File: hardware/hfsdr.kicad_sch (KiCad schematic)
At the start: 56 parts, among them J1 USB_C_Receptacle_USB2.0_16P, SW1 RST, SW2 BOOT0, SW4 EC12E2430803, U3 CH32V30xRxTx

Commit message: hardware fix: MCO MCK + MS5351 VDD
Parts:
- added JP1: MCK_OLD, symbol Jumper:SolderJumper_2_Open
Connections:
- net PA8 is gone; now on net MCK: TP18.1, U3.41 (PA8)
- net MCK: now also JP1.2 (B); no longer U3.37 (PC6)
- new net MCK_OLD: JP1.1 (A), U3.37 (PC6)
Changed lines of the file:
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@@
 	)
 	(junction
+		(at 120.65 85.09)
+		(diameter 0)
+		(color 0 0 0 0)
+	)
+	(junction
 		(at 158.75 46.99)
 		(diameter 0)
@@
 	)
 	(junction
+		(at 127 87.63)
+		(diameter 0)
+		(color 0 0 0 0)
+	)
+	(junction
 		(at 261.62 270.51)
 		(diameter 0)
@@
 	(wire
 		(pts
-			(xy 119.38 87.63) (xy 138.43 87.63)
+			(xy 119.38 87.63) (xy 127 87.63)
 		)
 		(stroke
@@
 	(wire
 		(pts
+			(xy 120.65 81.28) (xy 120.65 85.09)
+		)
+		(stroke
+			(width 0)
+			(type default)
+		)
+	)
+	(wire
+		(pts
 			(xy 158.75 46.99) (xy 158.75 49.53)
 		)
@@
 	(wire
 		(pts
+			(xy 101.6 81.28) (xy 120.65 81.28)
+		)
+		(stroke
+			(width 0)
+			(type default)
+		)
+	)
+	(wire
+		(pts
 			(xy 153.67 49.53) (xy 156.21 49.53)
 		)
@@
 	(wire
 		(pts
+			(xy 119.38 85.09) (xy 120.65 85.09)
+		)
+		(stroke
+			(width 0)
+			(type default)
+		)
+	)
+	(wire
+		(pts
 			(xy 332.74 68.58) (xy 332.74 64.77)
 		)
@@
 	(wire
 		(pts
+			(xy 127 87.63) (xy 138.43 87.63)
+		)
+		(stroke
+			(width 0)
+			(type default)
+		)
+	)
+	(wire
+		(pts
 			(xy 373.38 200.66) (xy 355.6 200.66)
 		)
@@
 	(wire
 		(pts
+			(xy 120.65 85.09) (xy 127 85.09)
+		)
+		(stroke
+			(width 0)
+			(type default)
+		)
+	)
+	(wire
+		(pts
 			(xy 168.91 85.09) (xy 180.34 85.09)
 		)
@@
 	(wire
 		(pts
+			(xy 127 85.09) (xy 127 87.63)
+		)
+		(stroke
+			(width 0)
+			(type default)
+		)
+	)
+	(wire
+		(pts
 			(xy 361.95 151.13) (xy 361.95 139.7)
 		)
@@
 		)
 	)
-	(global_label "MCK"
-		(shape input)
-		(at 171.45 82.55 0)
-		(fields_autoplaced yes)
-		(effects
-			(font
-				(size 1.27 1.27)
-			)
-			(justify left)
-		)
-		(property "Intersheetrefs" "${INTERSHEET_REFS}"
-			(at 178.4266 82.55 0)
-			(effects
-				(font
-					(size 1.27 1.27)
-				)
-				(justify left)
-				(hide yes)
-			)
-		)
-	)
 	(global_label "CS"
 		(shape input)
@@
 		)
 	)
+	(global_label "MCK_OLD"
+		(shape input)
+		(at 93.98 81.28 180)
+		(fields_autoplaced yes)
+		(effects
+			(font
+				(size 1.27 1.27)
+			)
+			(justify right)
+		)
+		(property "Intersheetrefs" "${INTERSHEET_REFS}"
+			(at 82.4072 81.28 0)
+			(effects
+				(font
+					(size 1.27 1.27)
+				)
+				(justify right)
+				(hide yes)
+			)
+		)
+	)
 	(global_label "ENC_A"
 		(shape input)
@@
 		)
 	)
+	(global_label "MCK_OLD"
+		(shape input)
+		(at 171.45 82.55 0)
+		(fields_autoplaced yes)
+		(effects
+			(font
+				(size 1.27 1.27)
+			)
+			(justify left)
+		)
+		(property "Intersheetrefs" "${INTERSHEET_REFS}"
+			(at 183.0228 82.55 0)
+			(effects
+				(font
+					(size 1.27 1.27)
+				)
+				(justify left)
+				(hide yes)
+			)
+		)
+	)
 	(global_label "PB2"
 		(shape input)
@@
 		)
 	)
+	(global_label "MCK"
+		(shape input)
+		(at 119.38 85.09 180)
+		(fields_autoplaced yes)
+		(effects
+			(font
+				(size 1.27 1.27)
+			)
+			(justify right)
+		)
+		(property "Intersheetrefs" "${INTERSHEET_REFS}"
+			(at 112.4034 85.09 0)
+			(effects
+				(font
+					(size 1.27 1.27)
+				)
+				(justify right)
+				(hide yes)
+			)
+		)
+	)
 	(global_label "ENC_B"
 		(shape input)
@@
 					(unit 1)
 				)
+			)
+		)
+	)
+	(symbol
+		(lib_id "Jumper:SolderJumper_2_Open")
+		(at 97.79 81.28 0)
+		(unit 1)
+		(exclude_from_sim no)
+		(in_bom no)
+		(on_board yes)
+		(dnp no)
+		(fields_autoplaced yes)
+		(property "Reference" "JP1"
+			(at 97.79 74.93 0)
+			(effects
+				(font
+					(size 1.27 1.27)
+				)
+			)
+		)
+		(property "Value" "MCK_OLD"
+			(at 97.79 77.47 0)
+			(effects
+				(font
+					(size 1.27 1.27)
+				)
+			)
+		)
+		(property "Footprint" ""
+			(at 97.79 81.28 0)
+			(effects
+				(font
+					(size 1.27 1.27)
+				)
+				(hide yes)
+			)
+		)
+		(property "Datasheet" "~"
+			(at 97.79 81.28 0)
+			(effects
+				(font
+					(size 1.27 1.27)
+				)
+				(hide yes)
+			)
+		)
+		(property "Description" "Solder Jumper, 2-pole, open"
+			(at 97.79 81.28 0)
+			(effects
+				(font
+					(size 1.27 1.27)
+				)
+				(hide yes)
+			)
+		)
+		(pin "2"
+		)
+		(pin "1"
+		)
+		(instances
+			(project ""
+				(path "/a11445ed-c3bd-4d1c-a039-1c09b0dceab8"
+					(reference "JP1")
+					(unit 1)
+				)

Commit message: feat: pcb edits
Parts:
- JP1: footprint (none) -> Jumper:SolderJumper-2_P1.3mm_Open_RoundedPad1.0x1.5mm
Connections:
- net +3.3V: now also FPC1.15, FPC1.16, FPC1.2; no longer FPC1.17, FPC1.3, FPC1.4
- net CS: now also FPC1.11; no longer FPC1.8
- net GND: now also FPC1.13, FPC1.14, FPC1.17, FPC1.7; no longer FPC1.12, FPC1.5, FPC1.6
- net PC10: now also FPC1.4; no longer FPC1.15
- net PC11: now also FPC1.8; no longer FPC1.11
- net RS: now also FPC1.12; no longer FPC1.7
- net SCL: now also FPC1.6; no longer FPC1.13
- net SCL_SCK: now also FPC1.10; no longer FPC1.9
- net SDA: now also FPC1.5; no longer FPC1.14
- net SDA_MOSI: now also FPC1.9; no longer FPC1.10
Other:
- moved on the sheet: FPC1
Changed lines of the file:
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@@
 	)
 	(junction
+		(at 355.6 190.5)
+		(diameter 0)
+		(color 0 0 0 0)
+	)
+	(junction
 		(at 332.74 38.1)
 		(diameter 0)
@@
 	)
 	(junction
-		(at 355.6 190.5)
+		(at 341.63 132.08)
 		(diameter 0)
 		(color 0 0 0 0)
 	)
 	(junction
-		(at 341.63 132.08)
+		(at 360.68 69.85)
 		(diameter 0)
 		(color 0 0 0 0)
 	)
 	(junction
-		(at 360.68 69.85)
+		(at 127 87.63)
 		(diameter 0)
 		(color 0 0 0 0)
 	)
 	(junction
-		(at 127 87.63)
+		(at 355.6 185.42)
 		(diameter 0)
 		(color 0 0 0 0)
@@
 	)
 	(junction
-		(at 360.68 62.23)
+		(at 355.6 195.58)
 		(diameter 0)
 		(color 0 0 0 0)
 	)
 	(junction
-		(at 236.22 262.89)
+		(at 360.68 62.23)
 		(diameter 0)
 		(color 0 0 0 0)
 	)
 	(junction
-		(at 355.6 195.58)
+		(at 236.22 262.89)
 		(diameter 0)
 		(color 0 0 0 0)
@@
 	(wire
 		(pts
+			(xy 355.6 185.42) (xy 355.6 187.96)
+		)
+		(stroke
+			(width 0)
+			(type default)
+		)
+	)
+	(wire
+		(pts
 			(xy 172.72 110.49) (xy 168.91 110.49)
 		)
@@
 			"////eQAAAA4AIAD/////////fwAAAAAAAACAeQAAAA8AIAD/////////fwAAAIAQAAAAeQAAABAA"
 			"IAD//39///9//wAAAAAAAAAAeQAAABEAIAD////////vf////////+//eQAAABIAIAAAPAAAADgA"
-			"AABAAAAAQgAAeQAAABMAIAB3JAAAKVMAAEg+AABIQgAAeQAAABQAIAAEAAAA//8AAA=="
+			"AABAAAAAQgAAeQAAABMAIAB3JAAAKVMAAEg+AABIQgAAeQAAABQAIAAEAAAA//8AAAAAAAAAAAAA"
+			"AAAAAAAAAAAAAAAAAAAAAAAAAAAAAAAAAAAAAAAAAAAAAAAAAAAAAAAAAAAAAAAAAAAAAAAAAAAA"
+			"AAAAAAAAAAAAAAAAAAAAAAAAAAAAAAAAAAAAAAAAAAAAAAAAAAAAAAAAAAAAAAAAAAAAAAAAAAAA"
+			"AAAAAAAAAAAAAAAAAAAAAAAAAAAAAAAAAAAAAAAAAAAAAAAAAAAAAAAAAAAAAAAAAAAAAAAAAAAA"
+			"AAAAAAAAAAAAAAAAAAAAAAAAAAAAAAAAAAAAAAAAAAAAAAAAAAAAAAAAAAAAAAAAAAAAAAAAAAAA"
+			"AAAAAAAAAAAAAAAAAAAAAAAAAAAAAAAAAAAAAAAAAAAAAAAAAAAAAAAAAAAAAAAAAAAAAAAAAAAA"
+			"AAAAAAAAAAAAAAAAAAAAAAAAAAAAAAAAAAAAAAAAAAAAAAAAAAAAAAAAAAAAAAAAAAAAAAAAAAAA"
+			"AAAAAAAAAAAAAAAAAAAAAAAAAAAAAAAAAAAAAAAAAAAAAAAAAAAAAAAAAAAAAAAAAAAAAAAAAAAA"
+			"AAAAAAAAAAAAAAAAAAAAAAAAAAAAAAAAAAAAAAAAAAAAAAAAAAAAAAAAAAAAAAAAAAAAAAAAAAAA"
+			"AAAAAAAAAAAAAAAAAAAAAAAAAAAAAAAAAAAAAAAAAAAAAAAAAAAAAAAAAAAAAAAAAAAAAAAAAAAA"
+			"AAAAAAAAAAAAAAAAAAAAAAAAAAAAAAAAAAAAAAAAAAAAAAAAAAAAAAAAAAAAAAAAAAAAAAAAAAAA"
+			"AAAAAAAAAAAAAAAAAAAAAAAAAAAAAAAAAAAAAAAAAAAAAAAAAAAAAAAAAAAAAAAAAAAAAAAAAAAA"
+			"AAAAAAAAAAAAAAAAAAAAAAAAAAAAAAAAAAAAAAAAAAAAAAAAAAAAAAAAAAAAAAAAAAAAAAAAAAAA"
+			"AAAAAAAAAAAAAAAAAAAAAAAAAAAAAAAAAAAAAAAAAAAAAAAAAAAAAAAAAAAAAAAAAAAAAAAAAAAA"
+			"AAAAAAAAAAAAAAAAAAAAAAAAAAAAAAAAAAAAAAAAAAAAAAAAAAAAAAAAAAAAAAAAAAAAAAAAAAAA"
+			"AAAAAAAAAAAAAAAAAAAAAAAAAAAAAAAAAAAAAAAAAAAAAAAAAAAAAAAAAAAAAAAAAAAAAAAAAAAA"
+			"AAAAAAAAAAAAAAAAAAAAAAAAAAAAAAAAAAAAAAAAAAAAAAAAAAAAAAAAAAAAAAAAAAAAAAAAAAAA"
+			"AAAAAAAAAAAAAAAAAAAAAAAAAAAAAAAAAAAAAAAAAAAAAAAAAAAAAAAAAAAAAAAAAAAAAAAAAAAA"
+			"AAAAAAAAAAAAAAAAAAAAAAAAAAAAAAAAAAAAAAAAAAAAAAAAAAAAAAAAAAAAAAAAAA=="
 		)
 	)
@@
 			"AAAAAAAAAAAAAAAAAAAAAAAAAAAAAAAAAAAAAAAAAAAAAAAAAAAAAAAAAAAAAAAAAAAAAAAAAAAA"
 			"AAAAAAAAAAAAAAAAAAAAAAAAAAAAAAAAAAAAAAAAAAAAAAAAAAAAAAAAAAAAAAAAAAAAAAAAAAAA"
+			"AAAAAAAAAAAAAAAAAAAAAAAAAAAAAAAAAAAAAAAAAAAAAAAAAAAAAAAAAAAAAAAAAAAAAAAAAAAA"
+			"AAAAAAAAAAAAAAAAAAAAAAAAAAAAAAAAAAAAAAAAAAAAAAAAAAAAAAAAAAAAAAAAAAAAAAAAAAAA"
+			"AAAAAAAAAAAAAAAAAAAAAAAAAAAAAAAAAAAAAAAAAAAAAAAAAAAAAAAAAAAAAAAAAAAAAAAAAAAA"
+			"AAAAAAAAAAAAAAAAAAAAAAAAAAAAAAAAAAAAAAAAAAAAAAAAAAAAAAAAAAAAAAAAAAAAAAAAAAAA"
+			"AAAAAAAAAAAAAAAAAAAAAAAAAAAAAAAAAAAAAAAAAAAAAAAAAAAAAAAAAAAAAAAAAAAAAAAAAAAA"
+			"AAAAAAAAAAAAAAAAAAAAAAAAAAAAAAAAAAAAAAAAAAAAAAAAAAAAAAAAAAAAAAAAAAAAAAAAAAAA"
+			"AAAAAAAAAAAAAAAAAAAAAAAAAAAAAAAAAAAAAAAAAAAAAAAAAAAAAAAAAAAAAAAAAAAAAAAAAAAA"
+			"AAAAAAAAAAAAAAAAAAAAAAAAAAAAAAAAAAAAAAAAAAAAAAAAAAAAAAAAAAAAAAAAAAAAAAAAAAAA"
+			"AAAAAAAAAAAAAAAAAAAAAAAAAAAAAAAAAAAAAAAAAAAAAAAAAAAAAAAAAAAAAAAAAAAAAAAAAAAA"
+			"AAAAAAAAAAAAAAAAAAAAAAAAAAAAAAAAAAAAAAAAAAAAAAAAAAAAAAAAAAAAAAAAAAAAAAAAAAAA"
+			"AAAAAAAAAAAAAAAAAAAAAAAAAAAAAAAAAAAAAAAAAAAAAAAAAAAAAAAAAAAAAAAAAAAAAAAAAAAA"
+			"AAAAAAAAAAAAAAAAAAAAAAAAAAAAAAAAAAAAAAAAAAAAAAAAAAAAAAAAAAAAAAAAAAAAAAAAAAAA"
+			"AAAAAAAAAAAAAAAAAAAAAAAAAAAAAAAAAAAAAAAAAAAAAAAAAAAAAAAAAAAAAAAAAAAAAAAAAAAA"
+			"AAAAAAAAAAAAAAAAAAAAAAAAAAAAAAAAAAAAAAAAAAAAAAAAAAAAAAAAAAAAAAAAAAAAAAAAAAAA"
+			"AAAAAAAAAAAAAAAAAAAAAAAAAAAAAAAAAAAAAAAAAAAAAAAAAAAAAAAAAAAAAAAAAAAAAAAAAAAA"
+			"AAAAAAAAAAAAAAAAAAAAAAAAAAAAAAAAAAAAAAAAAAAAAAAAAAAAAAAAAAAAAAAAAAAAAAAAAAAA"
+			"AAAAAAAAAAAAAAAAAAAAAAAAAAAAAAAAAAAAAAAAAAAAAAAAAAAAAAAAAAAAAAAAAAAAAAAAAAAA"
+			"AAAAAAAAAAAAAAAAAAAAAAAAAAAAAAAAAAAAAAAAAAAAAAAAAAAAAAAAAAAAAAAAAAAAAAAAAAAA"
 			"AAAAAAAAAAAAAAAAAAAAAAAAAAAAAAAAAAAAAAAAAAAAAAAAAA=="
 		)
@@
 			"gEQAEREAAEcAAAAngEQAEAAAACaARAAiIgAARwAAAAmARAAVAAAAJ4BEABAyAAAIAAAABwEAAEcA"
 			"AAAogEQAAQAAAD4CRAAAAAAARwAAAAiARAABAAAAKIBEAAAAAABHAAAAKYBEAAEAAAAHgEQAAAAA"
-			"AFsAAAAqgEQAAQAAAD4BYAAAAAAAKYBEAAAAAABHAA=="
+			"AFsAAAAqgEQAAQAAAD4BYAAAAAAAKYBEAAAAAABHAAAAAAAAAAAAAAAAAAAAAAAAAAAAAAAAAAAA"
+			"AAAAAAAAAAAAAAAAAAAAAAAAAAAAAAAAAAAAAAAAAAAAAAAAAAAAAAAAAAAAAAAAAAAAAAAAAAAA"
+			"AAAAAAAAAAAAAAAAAAAAAAAAAAAAAAAAAAAAAAAAAAAAAAAAAAAAAAAAAAAAAAAAAAAAAAAAAAAA"
+			"AAAAAAAAAAAAAAAAAAAAAAAAAAAAAAAAAAAAAAAAAAAAAAAAAAAAAAAAAAAAAAAAAAAAAAAAAAAA"
+			"AAAAAAAAAAAAAAAAAAAAAAAAAAAAAAAAAAAAAAAAAAAAAAAAAAAAAAAAAAAAAAAAAAAAAAAAAAAA"
+			"AAAAAAAAAAAAAAAAAAAAAAAAAAAAAAAAAAAAAAAAAAAAAAAAAAAAAAAAAAAAAAAAAAAAAAAAAAAA"
+			"AAAAAAAAAAAAAAAAAAAAAAAAAAAAAAAAAAAAAAAAAAAAAAAAAAAAAAAAAAAAAAAAAAAAAAAAAAAA"
+			"AAAAAAAAAAAAAAAAAAAAAAAAAAAAAAAAAAAAAAAAAAAAAAAAAAAAAAAAAAAAAAAAAAAAAAAAAAAA"
+			"AAAAAAAAAAAAAAAAAAAAAAAAAAAAAAAAAAAAAAAAAAAAAAAAAAAAAAAAAAAAAAAAAAAAAAAAAAAA"
+			"AAAAAAAAAAAAAAAAAAAAAAAAAAAAAAAAAAAAAAAAAAAAAAAAAAAAAAAAAAAAAAAAAAAAAAAAAAAA"
+			"AAAAAAAAAAAAAAAAAAAAAAAAAAAAAAAAAAAAAAAAAAAAAAAAAAAAAAAAAAAAAAAAAAAAAAAAAAAA"
+			"AAAAAAAAAAAAAAAAAAAAAAAAAAAAAAAAAAAAAAAAAAAAAAAAAAAAAAAAAAAAAAAAAAAAAAAAAAAA"
+			"AAAAAAAAAAAAAAAAAAAAAAAAAAAAAAAAAAAAAAAAAAAAAAAAAAAAAAAAAAAAAAAAAAAAAAAAAAAA"
+			"AAAAAAAAAAAAAAAAAAAAAAAAAAAAAAAAAAAAAAAAAAAAAAAAAAAAAAAAAAAAAAAAAAAAAAAAAAAA"
+			"AAAAAAAAAAAAAAAAAAAAAAAAAAAAAAAAAAAAAAAAAAAAAAAAAAAAAAAAAAAAAAAAAAAAAAAAAAAA"
+			"AAAAAAAAAAAAAAAAAAAAAAAAAAAAAAAAAAAAAAAAAAAAAAAAAAAAAAAAAAAAAAAAAAAAAAAAAAAA"
+			"AAAAAAAAAAAAAAAAAAAAAAAAAAAAAAAAAAAAAAAAAAAAAAAAAAAAAAAAAAAAAAAAAAAAAAAAAAAA"
+			"AAAAAAAAAAAAAAAAAAAAAAAAAAAAAAAAAAAAAAAAAAAAAAAAAAAAAAAAAAAAAAAAAAAAAAAAAAAA"
+			"AAAAAAAAAAAAAAAAAAAAAAAAAAAAAAAAAAAAAAAAAA=="
 		)
 	)
@@
 			"/yf/fwAA8N//J/9/AACQ4P8n/38AADDh/yf/fwAAEPj/J/9/AADA+P8n/38AAGD5/yf/fwAAEPr/"
 			"J/9/AACw+v8n/38AAGD7/yf/fwAAAPz/J/9/AACw/P8n/38AAFD9/yf/fwAAIP7/J/9/AADA/v8n"
-			"/38AAJD//yf/fwAAMAAAKP9/AADwAAAo/38AAJABACj/fw=="
+			"/38AAJD//yf/fwAAMAAAKP9/AADwAAAo/38AAJABACj/f0l2QXIvVDV1ZHErdFVldHhKbGdadDRI"
+			"WHI4TU16LzZKNjF2MHllTUdmVnNjdFhUeXh4cy9yR2c4R1JaSzh0ZEczYTlSOCt5c3VqbzRQaEYz"
+			"dW9CY0dyMTBUa2duR2Y4VjVXRlkzQXpRZU45N0RBWmZlMy9IVXNnd1VBWURrTzZBY0hOd1JxUklD"
+			"VGpmdTZPWlcrMTNUTTFtVkhVbWxoeDhrelhMV0dyWW5ienByZW12bzR5ZjZwOW4wU2dpNGp2V3lx"
+			"RGhRWGRoN2xaZjh1Q2ZzNk1LaWcxMUNYeWo5aDBzSEJHZ2RnaTdLeWlqNWtFRzQxZk5YUEhjU2dm"
+			"bjU0M2VFWDVWSmpCSTVDMkJIRmNOSlg2b0NqaXQ5L2t3NGJWOWgvZEtISG1NTEJVNlh6MWltT1hx"
+			"T3pxOXJCRDRGQUlLcEVxOCtpN3U4LytNWnI5L0x1dWlDN2RzRDdTUlVpVzd1cm9tTUR6eWVvQ1Z1"
+			"bk1oMXRBdWNtOW9RNi9rSlEzTmVpMlN2Q04vdXV4NUJSNDhhTjl1cmZ5ZG44Qzg0dHJEMis4UllI"
+			"b2l6U01ML2dOd3hHTm0zZnZ2ek0wV0xFcmgxYUNMelRDeTZmQ240N2ZtcGRRZnRCL2F5ODl5VjZq"
+			"MmovNHFmTjI1ZDRPaFdQRFpBdEZ2enBYUHg2VTNlUCtqMm1PTEpWMXg3MUsybUo0RmJqLzV6OVVT"
+			"L1NwOXIzZVpzKzdLdHpRZEplRzZxYU5zdG1aa280QU56WTJ2b2oybUdFbmVlUXRvdHZYSkhkREx5"
+			"WU9YTkdQZFFjUm1qQ0pZWXBOM21yN2xGRUwzZCsxeEg4K1kxeFl3RUdBRlFCRXg5TFg3MnNHTDJK"
+			"cys4clhEU2ViMTF1L2xRK3RXcUI4c0pMVmxtMk1ZaGh1bWI0NEo5MGYyeGRybCtNaTlvdFhSeklG"
+			"SlEyQURBY3E5ZFhmTnlMMjdLSmlubk5wRWcwVjZYRkFNY3hrZ1NSTG1aa2pOZTNKcG80azEwNmtF"
+			"NG1GYnJiV0Nab2l5SWduazE2eWNvMW02VVlEZ1NKQ1FXWW5oRm1ZVUU0TkNMYXR1TzFiNGovUi9h"
+			"U1F5QytDclQ1cklLUTNYN2lNVUZEeDhVRnJnay8vdVRJbml1Lzd1cjFTZHQvRnR5L24waGpoTG1s"
+			"NVh0M1NaalhNK05oZE9MamgxSm9hbGliWlVCVUFaTHNjT1BHalppWW1DOXRoUVp4VW1rMXJxSVRI"
+			"c1VXc29BWldsc2JWeUlYZFd4c3pIRklWY1k5akZWRFhZR2UyNXBEaTU4T1hYWHJkY1E2cjVZbnVr"
+			"MWV2R0x4eFBaMVNWd29MbGJzYkVaVWRBb05tTDZ0bzIwVg=="
 		)
 	)
@@
 			)
 		)
-		(property "Footprint" ""
+		(property "Footprint" "Jumper:SolderJumper-2_P1.3mm_Open_RoundedPad1.0x1.5mm"
 			(at 97.79 81.28 0)
 			(effects
@@
 	(symbol
 		(lib_id "easyeda:FPC-05F-18PH20")
-		(at 350.52 207.01 0)
-		(mirror y)
+		(at 350.52 207.01 180)
 		(unit 1)
 		(exclude_from_sim no)
@@
 		(dnp no)
 		(property "Reference" "FPC1"
-			(at 344.17 205.7399 0)
+			(at 344.17 208.2801 0)
 			(effects
 				(font
@@
 		)
 		(property "Value" "FPC-05F-18PH20"
-			(at 344.17 208.2799 0)
+			(at 344.17 205.7401 0)
 			(effects
 				(font
@@
 		)
 		(property "Footprint" "easyeda:FPC-SMD_18P-P0.50_FPC-05F-18PH20"
-			(at 350.52 241.3 0)
+			(at 350.52 172.72 0)
 			(effects
 				(font
@@
 		)
 		(property "LCSC Part" "C2856802"
-			(at 350.52 243.84 0)
+			(at 350.52 170.18 0)
 			(effects
 				(font
@@
 		)
 		(instances
-			(project ""
+			(project "hfsdr"
 				(path "/a11445ed-c3bd-4d1c-a039-1c09b0dceab8"
 					(reference "FPC1")

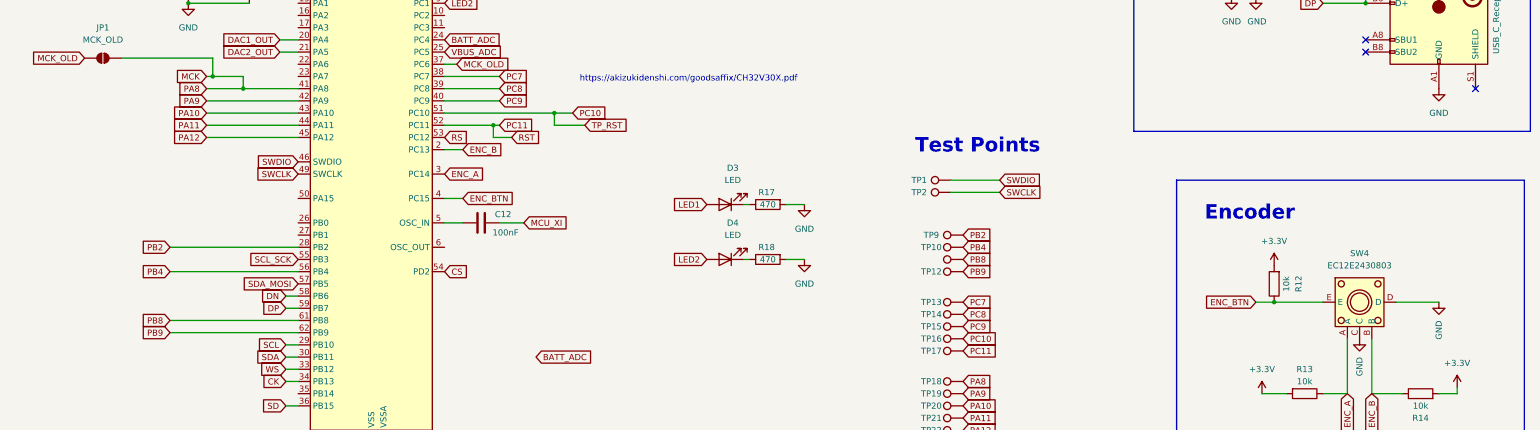
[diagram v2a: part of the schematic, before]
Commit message: hardware: rotary encoder to TIM10
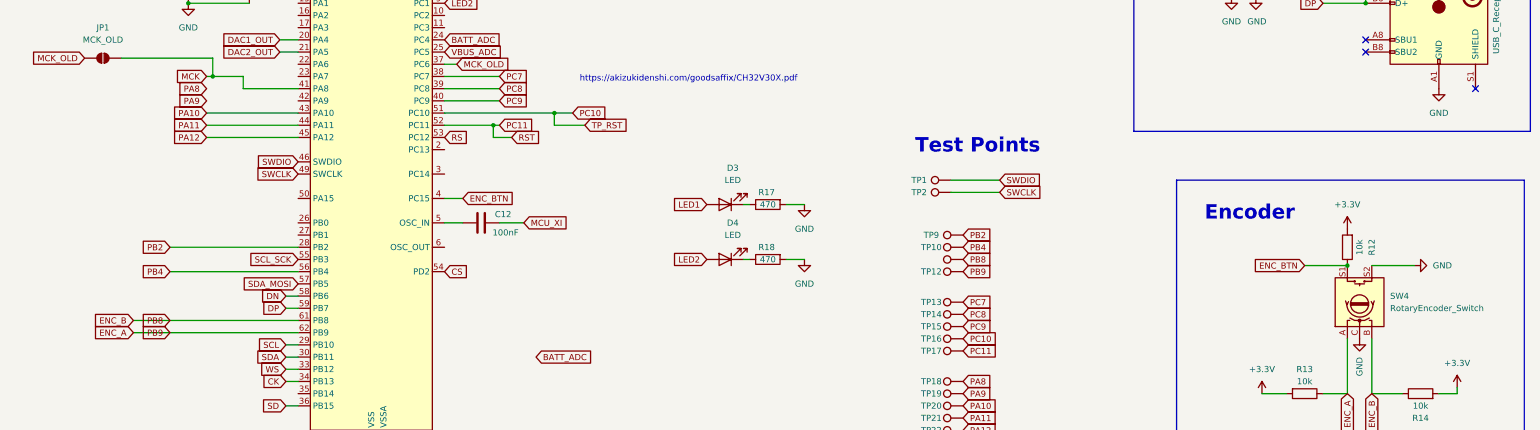
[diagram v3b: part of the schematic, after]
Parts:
- removed SW4: EC12E2430803, easyeda2kicad:SW-TH_EC12EXXXX, symbol easyeda2kicad:EC12E2430803
- added SW4: RotaryEncoder_Switch, Rotary_Encoder:RotaryEncoder_Alps_EC11E-Switch_Vertical_H20mm_MountingHoles, symbol Device:RotaryEncoder_Switch
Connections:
- net PB8 is gone; now on net ENC_B: TP11.1, U3.61 (PB8)
- net PB9 is gone; now on net ENC_A: TP12.1, U3.62 (PB9)
- net ENC_A: now also SW4.A; no longer U3.3 (PC14)
- net ENC_B: now also SW4.B; no longer U3.2 (PC13)
- net ENC_BTN: now also SW4.S1
- net GND: now also SW4.C, SW4.S2
- net MCK: no longer TP18.1
- net PA9: no longer U3.42 (PA9)
- new net PA8: TP18.1
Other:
- moved on the sheet: R12
